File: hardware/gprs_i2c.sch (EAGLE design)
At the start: 88 parts, among them IC1 SIM900, IC2 DS3231, J2 U.FL, Q2 PMBF170, Q3 PMBF170, Q4 si2305cd, Q5 si2305cd, T1 BC846, T2 BC846, T4 BC846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

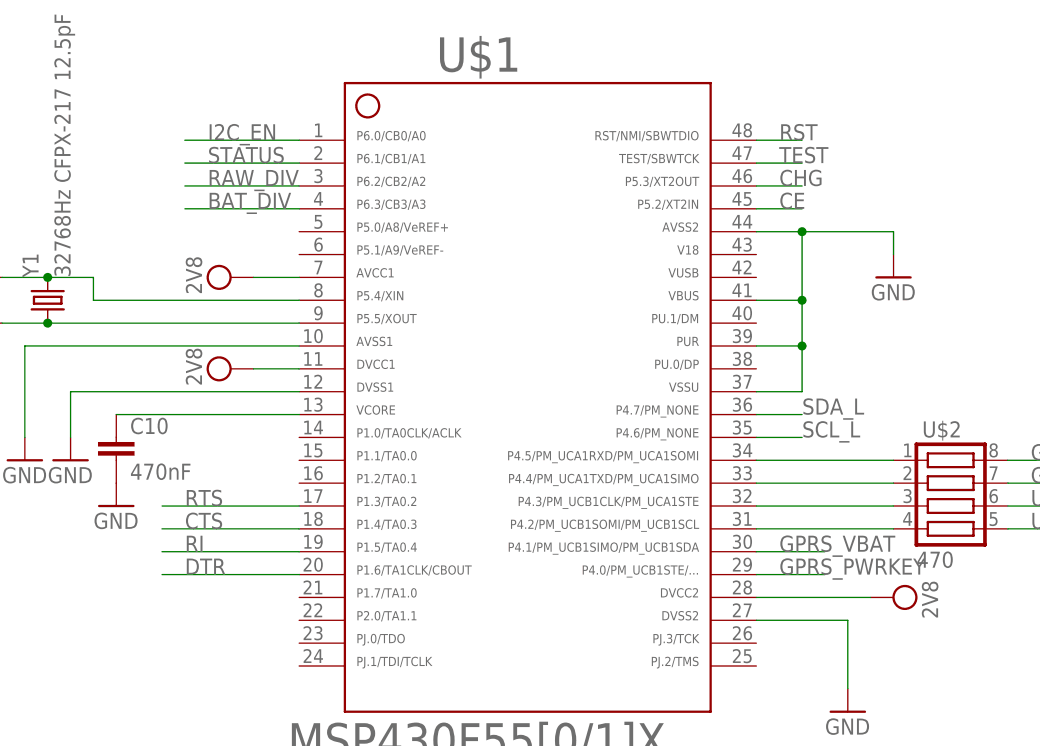
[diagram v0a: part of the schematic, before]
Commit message: move CE and CHG ports
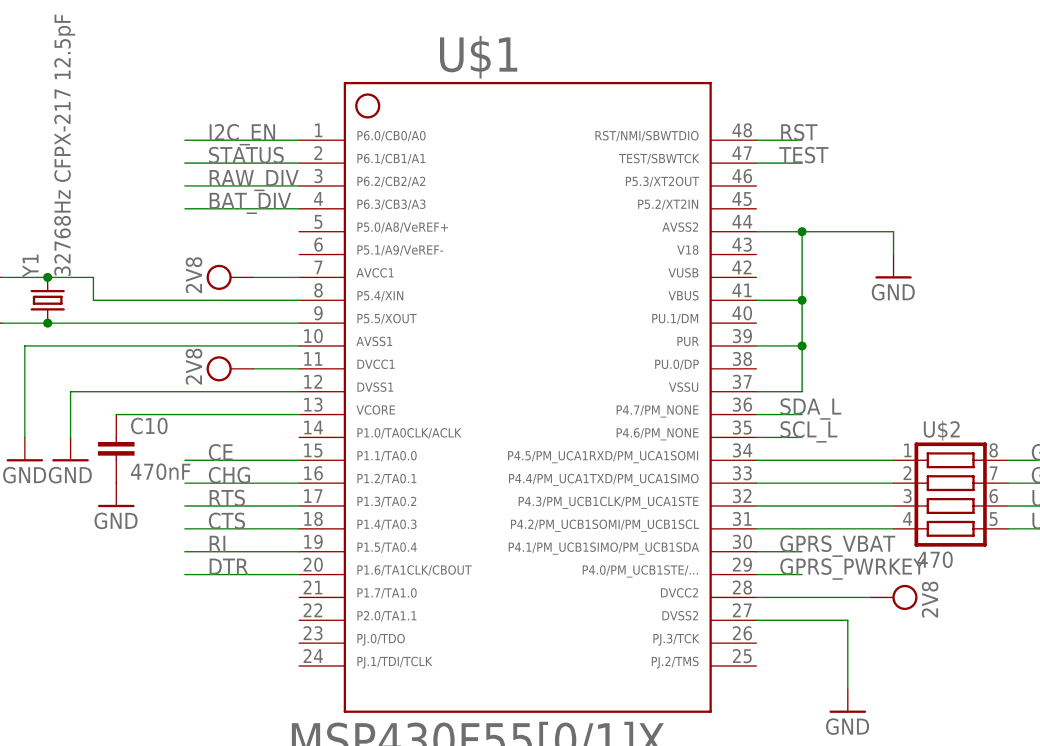
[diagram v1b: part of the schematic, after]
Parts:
- renumbered U$9 to U$5
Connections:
- net CE: now also U$1.15; no longer U$1.45
- net CHG: now also U$1.16; no longer U$1.46
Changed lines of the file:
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@@
 <part name="GND59" library="SparkFun" deviceset="GND" device=""/>
 <part name="GND61" library="SparkFun" deviceset="GND" device=""/>
-<part name="U$9" library="Simplex-Fuses" deviceset="RESETTABLE" device="_0805"/>
 <part name="C3" library="rcl" deviceset="C-EU" device="C0805" value="10uF"/>
 <part name="GND42" library="SparkFun" deviceset="GND" device=""/>
@@
 <part name="C7" library="rcl" deviceset="C-EU" device="C1206" value="10uF"/>
 <part name="GND23" library="SparkFun" deviceset="GND" device=""/>
+<part name="U$5" library="Simplex-Fuses" deviceset="RESETTABLE" device="_0805"/>
 </parts>
 <sheets>
@@
 <instance part="GND59" gate="1" x="381" y="271.78"/>
 <instance part="GND61" gate="1" x="345.44" y="271.78"/>
-<instance part="U$9" gate="G$1" x="142.24" y="292.1"/>
 <instance part="C3" gate="G$1" x="33.02" y="279.4"/>
 <instance part="GND42" gate="1" x="134.62" y="81.28"/>
@@
 <instance part="C7" gate="G$1" x="91.44" y="279.4"/>
 <instance part="GND23" gate="1" x="91.44" y="266.7"/>
+<instance part="U$5" gate="G$1" x="142.24" y="292.1"/>
 </instances>
 <busses>
@@
 <pinref part="U$6" gate="G$1" pin="IN"/>
 <wire x1="147.32" y1="292.1" x2="162.56" y2="292.1" width="0.1524" layer="91"/>
-<pinref part="U$9" gate="G$1" pin="P$2"/>
+<pinref part="U$5" gate="G$1" pin="P$2"/>
 </segment>
 <segment>
@@
 </segment>
 <segment>
-<pinref part="U$1" gate="G$1" pin="45"/>
-<wire x1="396.24" y1="172.72" x2="401.32" y2="172.72" width="0.1524" layer="91"/>
-<label x="398.78" y="172.72" size="1.778" layer="95"/>
+<pinref part="U$1" gate="G$1" pin="15"/>
+<wire x1="345.44" y1="144.78" x2="332.74" y2="144.78" width="0.1524" layer="91"/>
+<label x="335.28" y="144.78" size="1.778" layer="95"/>
 </segment>
 </net>
@@
 <segment>
 <pinref part="U$1" gate="G$1" pin="29"/>
-<wire x1="396.24" y1="132.08" x2="403.86" y2="132.08" width="0.1524" layer="91"/>
+<wire x1="396.24" y1="132.08" x2="401.32" y2="132.08" width="0.1524" layer="91"/>
 <label x="398.78" y="132.08" size="1.778" layer="95"/>
 </segment>
@@
 <segment>
 <pinref part="U$1" gate="G$1" pin="18"/>
-<wire x1="330.2" y1="137.16" x2="345.44" y2="137.16" width="0.1524" layer="91"/>
-<label x="332.74" y="137.16" size="1.778" layer="95"/>
+<wire x1="332.74" y1="137.16" x2="345.44" y2="137.16" width="0.1524" layer="91"/>
+<label x="335.28" y="137.16" size="1.778" layer="95"/>
 </segment>
 </net>
@@
 <segment>
 <pinref part="U$1" gate="G$1" pin="17"/>
-<wire x1="345.44" y1="139.7" x2="330.2" y2="139.7" width="0.1524" layer="91"/>
-<label x="332.74" y="139.7" size="1.778" layer="95"/>
+<wire x1="345.44" y1="139.7" x2="332.74" y2="139.7" width="0.1524" layer="91"/>
+<label x="335.28" y="139.7" size="1.778" layer="95"/>
 </segment>
 </net>
@@
 <segment>
 <pinref part="U$1" gate="G$1" pin="20"/>
-<wire x1="345.44" y1="132.08" x2="330.2" y2="132.08" width="0.1524" layer="91"/>
-<label x="332.74" y="132.08" size="1.778" layer="95"/>
+<wire x1="345.44" y1="132.08" x2="332.74" y2="132.08" width="0.1524" layer="91"/>
+<label x="335.28" y="132.08" size="1.778" layer="95"/>
 </segment>
 </net>
@@
 <segment>
 <pinref part="U$1" gate="G$1" pin="19"/>
-<wire x1="330.2" y1="134.62" x2="345.44" y2="134.62" width="0.1524" layer="91"/>
-<label x="332.74" y="134.62" size="1.778" layer="95"/>
+<wire x1="332.74" y1="134.62" x2="345.44" y2="134.62" width="0.1524" layer="91"/>
+<label x="335.28" y="134.62" size="1.778" layer="95"/>
 </segment>
 </net>
@@
 <segment>
 <pinref part="U$1" gate="G$1" pin="30"/>
-<wire x1="396.24" y1="134.62" x2="403.86" y2="134.62" width="0.1524" layer="91"/>
+<wire x1="396.24" y1="134.62" x2="401.32" y2="134.62" width="0.1524" layer="91"/>
 <label x="398.78" y="134.62" size="1.778" layer="95"/>
 </segment>
@@
 </segment>
 <segment>
-<pinref part="U$1" gate="G$1" pin="46"/>
-<wire x1="396.24" y1="175.26" x2="401.32" y2="175.26" width="0.1524" layer="91"/>
-<label x="398.78" y="175.26" size="1.778" layer="95"/>
+<pinref part="U$1" gate="G$1" pin="16"/>
+<wire x1="345.44" y1="142.24" x2="332.74" y2="142.24" width="0.1524" layer="91"/>
+<label x="335.28" y="142.24" size="1.778" layer="95"/>
 </segment>
 </net>
@@
 <pinref part="U$1" gate="G$1" pin="35"/>
 <wire x1="396.24" y1="147.32" x2="401.32" y2="147.32" width="0.1524" layer="91"/>
-<label x="401.32" y="147.32" size="1.778" layer="95"/>
+<label x="398.78" y="147.32" size="1.778" layer="95"/>
 </segment>
 <segment>
@@
 <pinref part="U$1" gate="G$1" pin="36"/>
 <wire x1="396.24" y1="149.86" x2="401.32" y2="149.86" width="0.1524" layer="91"/>
-<label x="401.32" y="149.86" size="1.778" layer="95"/>
+<label x="398.78" y="149.86" size="1.778" layer="95"/>
 </segment>
 <segment>
@@
 <wire x1="137.16" y1="292.1" x2="127" y2="292.1" width="0.1524" layer="91"/>
 <label x="127" y="292.1" size="1.778" layer="95"/>
-<pinref part="U$9" gate="G$1" pin="P$1"/>
-</segment>
-<segment>
+<pinref part="U$5" gate="G$1" pin="P$1"/>
+</segment>
+<segment>

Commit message: pcb verified
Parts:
- added R5: 470, rcl:R-EU_R0805W
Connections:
- new net N$11: R5.2, U$1.15
- net CE: now also R5.1; no longer U$1.15
- net GND: now also U$18.4, U$18.5
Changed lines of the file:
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@@
 <part name="GND23" library="SparkFun" deviceset="GND" device=""/>
 <part name="U$5" library="Simplex-Fuses" deviceset="RESETTABLE" device="_0805"/>
+<part name="GND43" library="SparkFun" deviceset="GND" device=""/>
+<part name="R5" library="rcl" deviceset="R-EU_" device="R0805W" value="470"/>
 </parts>
 <sheets>
@@
 <instance part="GND23" gate="1" x="91.44" y="266.7"/>
 <instance part="U$5" gate="G$1" x="142.24" y="292.1"/>
+<instance part="GND43" gate="1" x="223.52" y="116.84"/>
+<instance part="R5" gate="G$1" x="340.36" y="144.78"/>
 </instances>
 <busses>
@@
 <wire x1="91.44" y1="274.32" x2="91.44" y2="269.24" width="0.1524" layer="91"/>
 </segment>
+<segment>
+<pinref part="U$18" gate="G$1" pin="5"/>
+<pinref part="GND43" gate="1" pin="GND"/>
+<wire x1="215.9" y1="134.62" x2="223.52" y2="134.62" width="0.1524" layer="91"/>
+<wire x1="223.52" y1="134.62" x2="223.52" y2="121.92" width="0.1524" layer="91"/>
+<pinref part="U$18" gate="G$1" pin="4"/>
+<wire x1="223.52" y1="121.92" x2="223.52" y2="119.38" width="0.1524" layer="91"/>
+<wire x1="215.9" y1="121.92" x2="223.52" y2="121.92" width="0.1524" layer="91"/>
+<junction x="223.52" y="121.92"/>
+</segment>
 </net>
 <net name="VIN" class="0">
@@
 </segment>
 <segment>
-<pinref part="U$1" gate="G$1" pin="15"/>
-<wire x1="345.44" y1="144.78" x2="332.74" y2="144.78" width="0.1524" layer="91"/>
-<label x="335.28" y="144.78" size="1.778" layer="95"/>
+<wire x1="335.28" y1="144.78" x2="330.2" y2="144.78" width="0.1524" layer="91"/>
+<label x="332.74" y="144.78" size="1.778" layer="95"/>
+<pinref part="R5" gate="G$1" pin="1"/>
 </segment>
 </net>
@@
 </segment>
 </net>
+<net name="N$11" class="0">
+<segment>
+<pinref part="U$1" gate="G$1" pin="15"/>
+<pinref part="R5" gate="G$1" pin="2"/>
+</segment>
+</net>
